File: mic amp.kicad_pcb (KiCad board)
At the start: 2 copper layers, 71 x 34 mm, 26 parts, among them P1 BNC, SW1 DPDT, U1 LME49710, U2 LF356

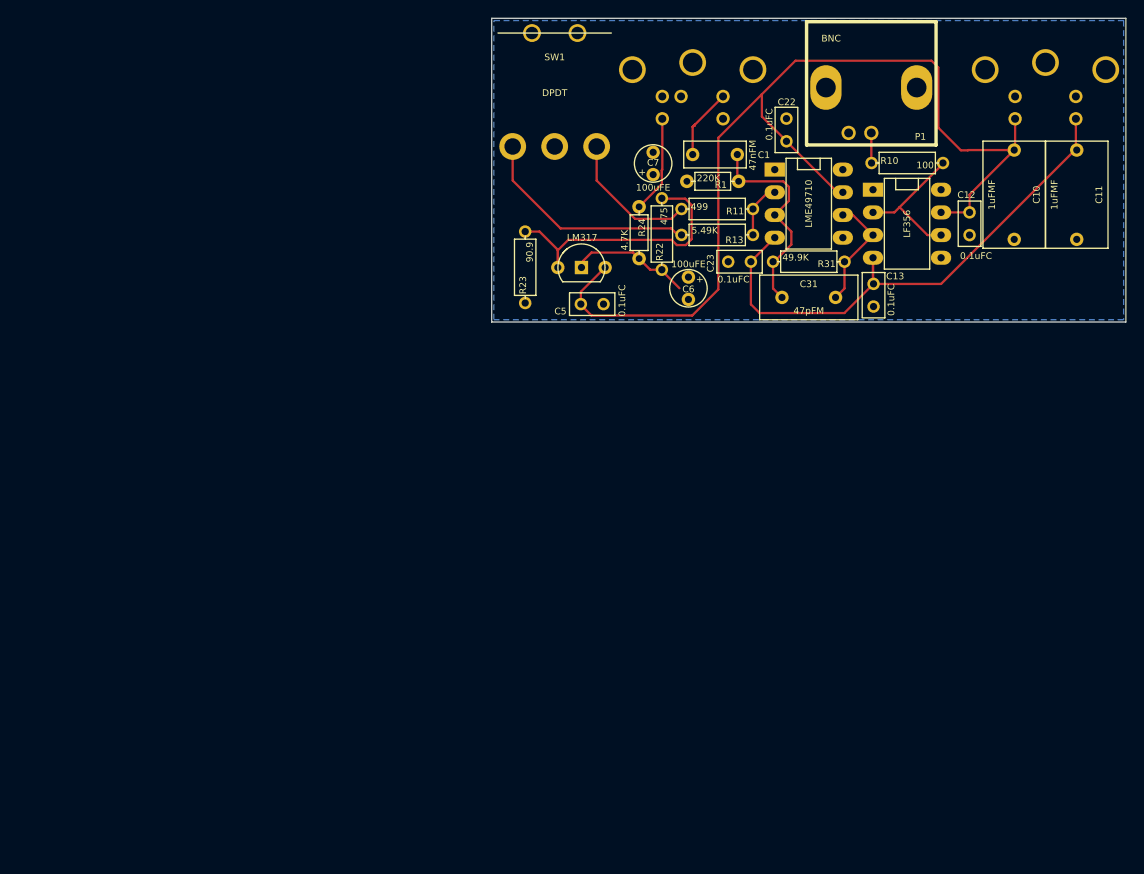
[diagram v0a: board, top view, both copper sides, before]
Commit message: ENH: Updated through-hole version
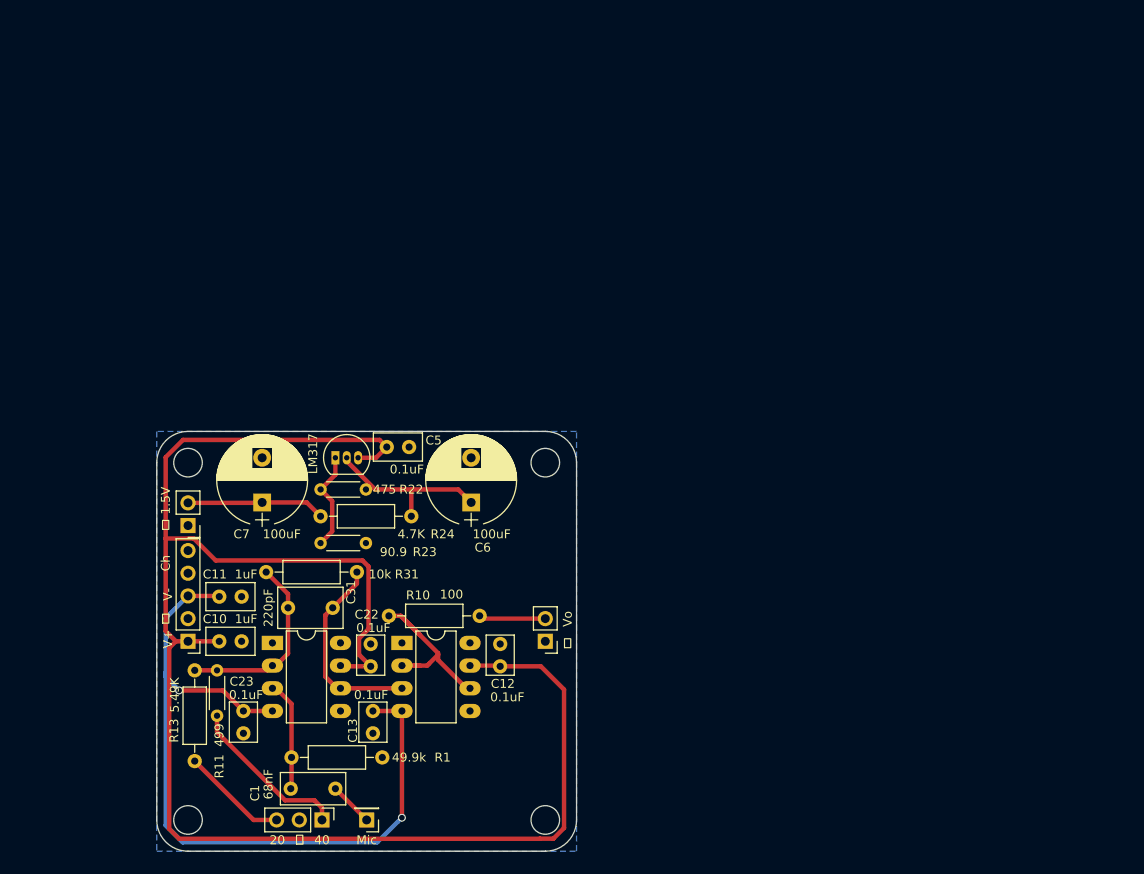
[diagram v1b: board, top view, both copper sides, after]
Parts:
- removed MIC1: 5P_miniDIN, LBHB:mini-DIN-5-pin
- removed P1: BNC, LBHB:BNC_socket_Amphenol
- removed PWR1: PWR, LBHB:mini-DIN-4-pin
- removed SW1: DPDT, LBHB:switch-SPDT-7101
- added J1: CONN_01X02, Conn_PinSocket_2.54mm:PinSocket_1x02_P2.54mm_Vertical, F.Cu at (100.0, 107.0)
- added J2: CONN_01X01, Conn_PinSocket_2.54mm:PinSocket_1x01_P2.54mm_Vertical, F.Cu at (120.0, 140.0)
- added J3: CONN_01X03, Conn_PinSocket_2.54mm:PinSocket_1x03_P2.54mm_Vertical, F.Cu at (115.0, 140.0)
- added J4: CONN_01X01, MountingHole:MountingHole_3.2mm_M3, F.Cu at (100.0, 140.0)
- added J5: CONN_01X01, MountingHole:MountingHole_3.2mm_M3, F.Cu at (140.0, 100.0)
- added J6: CONN_01X01, MountingHole:MountingHole_3.2mm_M3, F.Cu at (100.0, 100.0)
- added J7: CONN_01X01, MountingHole:MountingHole_3.2mm_M3, F.Cu at (140.0, 140.0)
- added J8: CONN_01X02, Conn_PinSocket_2.54mm:PinSocket_1x02_P2.54mm_Vertical, F.Cu at (140.0, 120.0)
- added J9: CONN_01X05, Conn_PinSocket_2.54mm:PinSocket_1x05_P2.54mm_Vertical, F.Cu at (100.0, 120.0)
- C1: value 47nFM -> 68nF; footprint LBHB:capacitor-7x3mm-L_5mm -> Capacitor_THT:C_Rect_L7.2mm_W3.5mm_P5.00mm_FKS2_FKP2_MKS2_MKP2
- C10, C11: value 1uFMF -> 1uF; footprint LBHB:capacitor-7x12mm-L_10mm -> custom:C_Rect_L5.5mm_W3.15mm_P2.50mm
- C12, C13, C22, C23: value 0.1uFC -> 0.1uF; footprint LBHB:capacitor-2.5x5mm-L_2.5mm -> custom:C_Rect_L4.5mm_W3.15mm_P2.50mm
- C31: value 47pFM -> 220pF; footprint LBHB:capacitor-5x11mm-L_6mm -> Capacitor_THT:C_Rect_L7.2mm_W4.5mm_P5.00mm_FKS2_FKP2_MKS2_MKP2
- C5: value 0.1uFC -> 0.1uF; footprint LBHB:capacitor-2.5x5mm-L_2.5mm -> custom:C_Rect_L5.5mm_W3.15mm_P2.50mm
- C6, C7: value 100uFE -> 100uF; footprint LBHB:capacitor-D_4mm-L_2.4mm -> Capacitor_THT:CP_Radial_D10.0mm_P5.00mm
- R1: value 220K -> 49.9k; footprint LBHB:resistor-4x2mm -> Resistor_THT:R_Axial_DIN0207_L6.3mm_D2.5mm_P10.16mm_Horizontal
- R10, R13: footprint LBHB:resistor-6.3x2.4mm -> Resistor_THT:R_Axial_DIN0207_L6.3mm_D2.5mm_P10.16mm_Horizontal
- R11, R22, R23: footprint LBHB:resistor-6.3x2.4mm -> Resistor_THT:R_Axial_DIN0204_L3.6mm_D1.6mm_P5.08mm_Horizontal
- R24: footprint LBHB:resistor-4x2mm -> Resistor_THT:R_Axial_DIN0207_L6.3mm_D2.5mm_P10.16mm_Horizontal
- R31: value 49.9K -> 10k; footprint LBHB:resistor-6.3x2.4mm -> Resistor_THT:R_Axial_DIN0207_L6.3mm_D2.5mm_P10.16mm_Horizontal
- U1: value LME49710 -> LF356; footprint LBHB:DIP-8 -> Package_DIP:DIP-8_W7.62mm_LongPads
- U2: footprint LBHB:DIP-8 -> Package_DIP:DIP-8_W7.62mm_LongPads
- VREG1: footprint LBHB:TO-92-LM317 -> Package_TO_SOT_THT:TO-92_Inline_Narrow_Oval
- moved C11 104.9 mm to (104.8, 115.0), turned to 0 degrees
- moved C10 101.0 mm to (104.8, 120.0), turned to 0 degrees
- moved C1 85.4 mm to (111.5, 136.5)
- moved R13 83.0 mm to (100.8, 133.4), turned to 90 degrees
- moved R11 79.7 mm to (103.2, 128.3), turned to 90 degrees
- moved U1 77.6 mm to (109.5, 120.2), turned to 0 degrees
- moved R10 77.1 mm to (122.5, 117.2), turned to 0 degrees
- moved C23 75.8 mm to (106.2, 129.1), turned to 90 degrees
- moved C22 75.0 mm to (120.5, 121.5)
- moved R1 74.4 mm to (121.8, 133.0), turned to 180 degrees
- moved C13 73.7 mm to (120.7, 129.1)
- moved U2 73.5 mm to (124.0, 120.2), turned to 0 degrees
- moved C12 71.4 mm to (134.9, 121.5), turned to 270 degrees
- moved R31 70.0 mm to (108.8, 112.2)
- moved C31 63.6 mm to (116.2, 116.2)
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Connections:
- C31 pad 2: Net-(C1-Pad1) -> Net-(C31-Pad2)
- R11 pad 2: Net-(R11-Pad2) -> Net-(C31-Pad2)
- R13 pad 2: Net-(R11-Pad2) -> Net-(C31-Pad2)
- R31 pad 1: Net-(C1-Pad1) -> Net-(C31-Pad2)
- U1 pad 2: Net-(R11-Pad2) -> Net-(C31-Pad2)
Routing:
- net +15V: track 115.2 -> 188.7 mm
- net -15V: track 62.4 -> 87.8 mm, vias 0 -> 2
- net Net-(C31-Pad2): track 0.00 -> 21.4 mm
- net Net-(R22-Pad1): track 31.8 -> 11.3 mm
- net Net-(J3-Pad3): track 25.2 -> 11.9 mm
- net Net-(C1-Pad1): track 25.1 -> 12.4 mm
- net Net-(C31-Pad1): track 13.4 -> 22.3 mm
- net Net-(R10-Pad1): track 15.7 -> 22.5 mm
- net Net-(R11-Pad2): track 6.41 -> 0.00 mm
- net Net-(C6-Pad1): track 13.8 -> 19.2 mm
- net Net-(C7-Pad1): track 11.6 -> 15.5 mm
- net Net-(J8-Pad2): track 3.83 -> 7.48 mm
- net Net-(C1-Pad2): track 8.32 -> 4.95 mm
- net Net-(J3-Pad1): track 15.5 -> 18.6 mm
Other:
- board size 71 x 34 mm -> 47 x 47 mm
- net class Default: clearance 0.254 -> 0.25; trace_width 0.254 -> 0.5
- rule trace_clearance: 0.254 -> 0.25
- board text added: "1.5V"
- board text added: "20"
- board text added: "40"
- board text added: "Ch"
- board text added: "LBHB@OHSU BSD"
- board text added: "Mic"
- board text added: "V+"
- board text added: "V-"
- board text added: "Vo"
- board text added: "⏚"

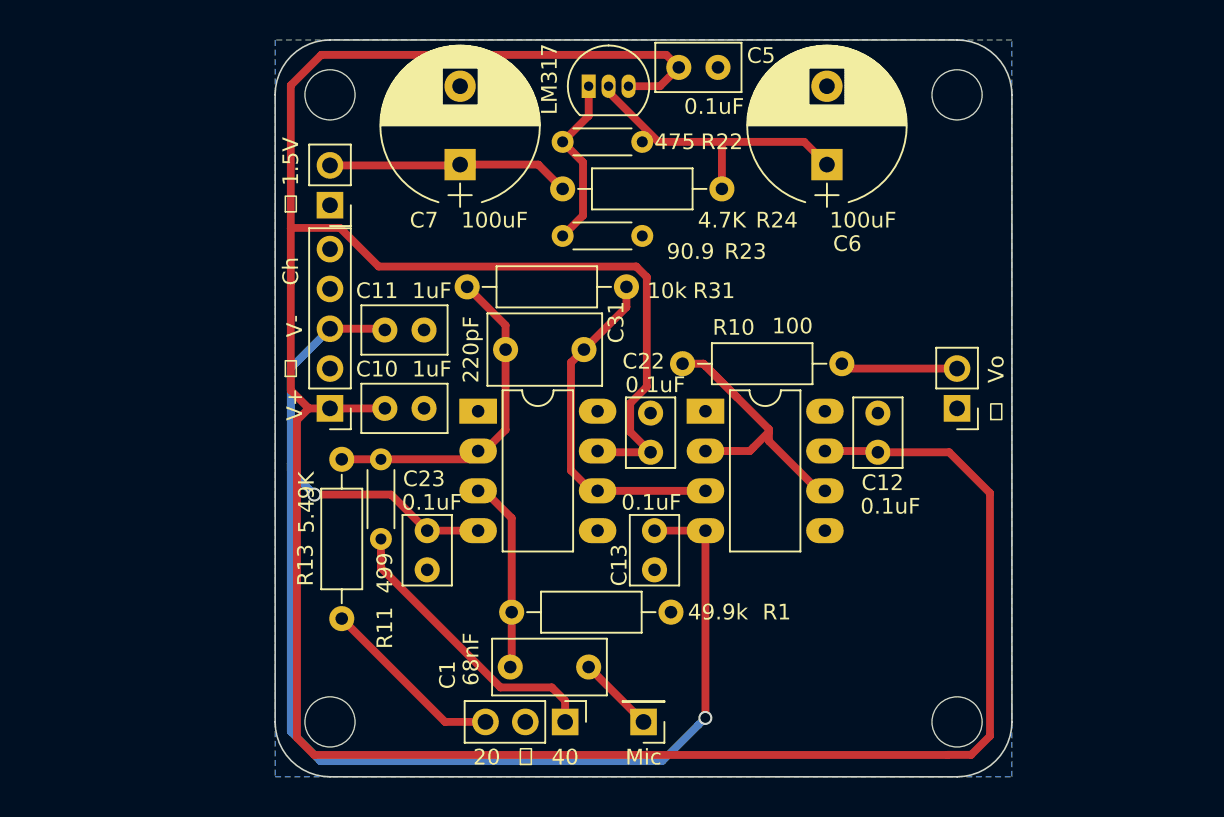
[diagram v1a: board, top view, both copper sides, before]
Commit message: Through-hole version of mic amp
Printed via OSH park. Part list availbale via Mouser (see 171218 mic amp
project). Designed to fit a Hammond enclosure that accomodates 75mm wide
PCBs.
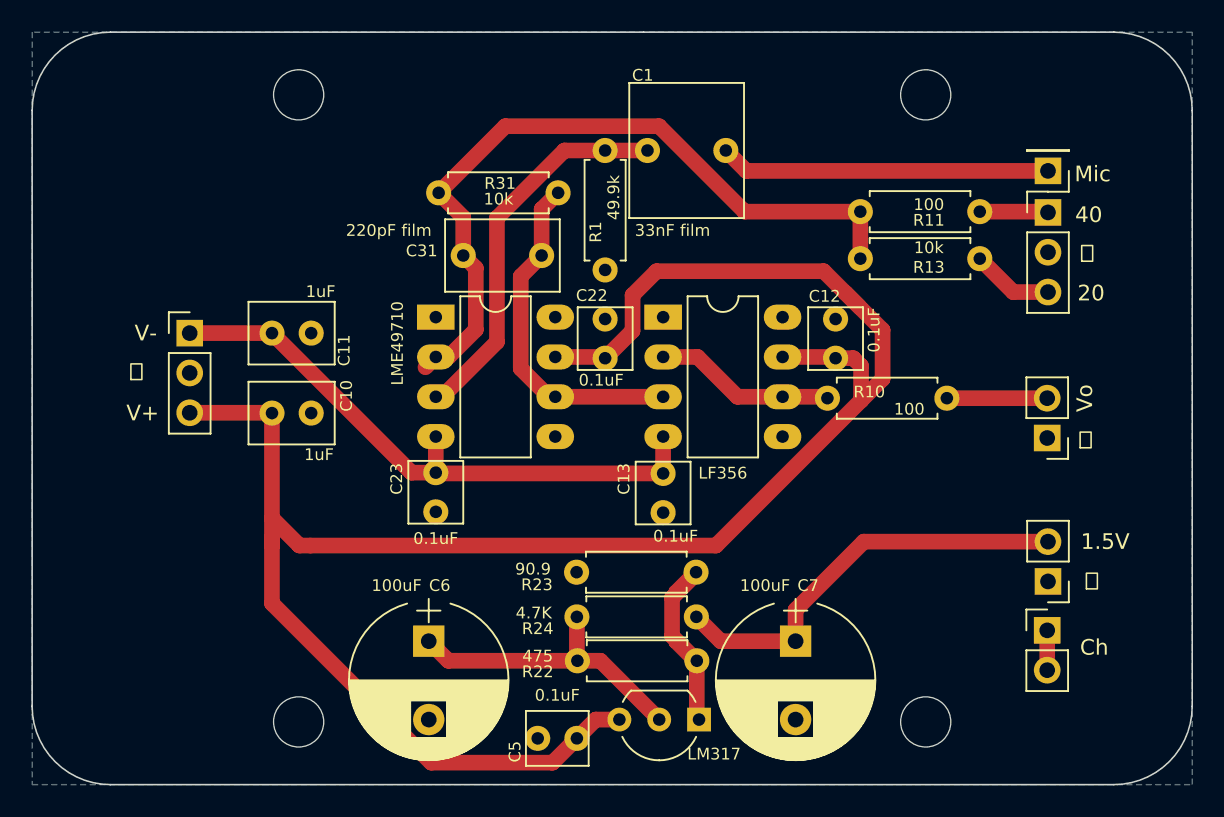
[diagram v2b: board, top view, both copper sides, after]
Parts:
- added J10: CONN_01X02, Conn_PinSocket_2.54mm:PinSocket_1x02_P2.54mm_Vertical, F.Cu at (145.8, 134.2)
- C1: value 68nF -> 33nF film; footprint Capacitor_THT:C_Rect_L7.2mm_W3.5mm_P5.00mm_FKS2_FKP2_MKS2_MKP2 -> Capacitor_THT:C_Rect_L7.2mm_W8.5mm_P5.00mm_FKP2_FKP2_MKS2_MKP2
- C10, C11: footprint custom:C_Rect_L5.5mm_W3.15mm_P2.50mm -> custom:C_Rect_L5.5mm_W4.0mm_P2.50mm
- C12, C13, C22, C23: footprint custom:C_Rect_L4.5mm_W3.15mm_P2.50mm -> custom:C_Rect_L4.0mm_W3.5mm_P2.50mm
- C31: value 220pF -> 220pF film
- C5: footprint custom:C_Rect_L5.5mm_W3.15mm_P2.50mm -> custom:C_Rect_L4.0mm_W3.5mm_P2.50mm
- J9: value CONN_01X05 -> CONN_01X03; footprint Conn_PinSocket_2.54mm:PinSocket_1x05_P2.54mm_Vertical -> Conn_PinSocket_2.54mm:PinSocket_1x03_P2.54mm_Vertical
- R1, R10, R24, R31: footprint Resistor_THT:R_Axial_DIN0207_L6.3mm_D2.5mm_P10.16mm_Horizontal -> Resistor_THT:R_Axial_DIN0207_L6.3mm_D2.5mm_P7.62mm_Horizontal
- R11: value 499 -> 100; footprint Resistor_THT:R_Axial_DIN0204_L3.6mm_D1.6mm_P5.08mm_Horizontal -> Resistor_THT:R_Axial_DIN0207_L6.3mm_D2.5mm_P7.62mm_Horizontal
- R13: value 5.49K -> 10k; footprint Resistor_THT:R_Axial_DIN0207_L6.3mm_D2.5mm_P10.16mm_Horizontal -> Resistor_THT:R_Axial_DIN0207_L6.3mm_D2.5mm_P7.62mm_Horizontal
- R22, R23: footprint Resistor_THT:R_Axial_DIN0204_L3.6mm_D1.6mm_P5.08mm_Horizontal -> Resistor_THT:R_Axial_DIN0207_L6.3mm_D2.5mm_P7.62mm_Horizontal
- U1: value LF356 -> LME49710
- VREG1: footprint Package_TO_SOT_THT:TO-92_Inline_Narrow_Oval -> Package_TO_SOT_THT:TO-92_Inline_Wide
- moved J1 51.7 mm to (145.8, 131.0)
- moved R13 46.7 mm to (141.4, 110.5), turned to 180 degrees
- moved J3 44.8 mm to (145.8, 107.5), turned to 0 degrees
- moved C5 43.7 mm to (114.5, 141.1), turned to 180 degrees
- moved J2 43.6 mm to (145.8, 104.8)
- moved R11 43.5 mm to (141.4, 107.5), turned to 180 degrees
- moved VREG1 41.0 mm to (123.5, 139.8), turned to 180 degrees
- moved C6 39.6 mm to (106.3, 134.8), turned to 270 degrees
- moved C7 37.2 mm to (129.7, 134.8), turned to 270 degrees
- moved R22 34.2 mm to (123.4, 136.1), turned to 180 degrees
- moved C1 34.1 mm to (120.2, 103.5)
- moved R24 28.8 mm to (115.8, 133.3), turned to 0 degrees
- moved R23 23.1 mm to (123.3, 130.4), turned to 180 degrees
- moved R1 22.2 mm to (117.5, 111.2), turned to 90 degrees
- moved J9 10.2 mm to (91.0, 115.2), turned to 0 degrees
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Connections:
- J9 pad 1: +15V -> -15V
- J9 pad 3: -15V -> +15V
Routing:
- net +15V: track 188.7 -> 129.7 mm
- net -15V: track 87.8 -> 38.6 mm, vias 2 -> 0
- net Net-(C31-Pad2): track 21.4 -> 48.6 mm
- net Net-(C7-Pad1): track 15.5 -> 34.1 mm
- net Net-(C1-Pad2): track 4.95 -> 21.1 mm
- net Net-(J3-Pad1): track 18.6 -> 4.37 mm
- net Net-(C1-Pad1): track 12.4 -> 24.7 mm
- net Net-(R10-Pad1): track 22.5 -> 12.3 mm
- net Net-(J3-Pad3): track 11.9 -> 5.23 mm
- net Net-(R22-Pad1): track 11.3 -> 17.8 mm
- net Net-(J10-Pad1): track 0.00 -> 2.54 mm
- net Net-(J8-Pad2): track 7.48 -> 6.40 mm
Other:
- board size 47 x 47 mm -> 74 x 48 mm
- net class Default: trace_width 0.5 -> 1
- board text added: "Microphone amplifier 2017.12.18 revision Brad Buran LBHB@OHSU"
- board text removed: "LBHB@OHSU BSD"
